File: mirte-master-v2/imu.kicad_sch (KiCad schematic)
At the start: 1 part, among them J8 IMU MPU-9250

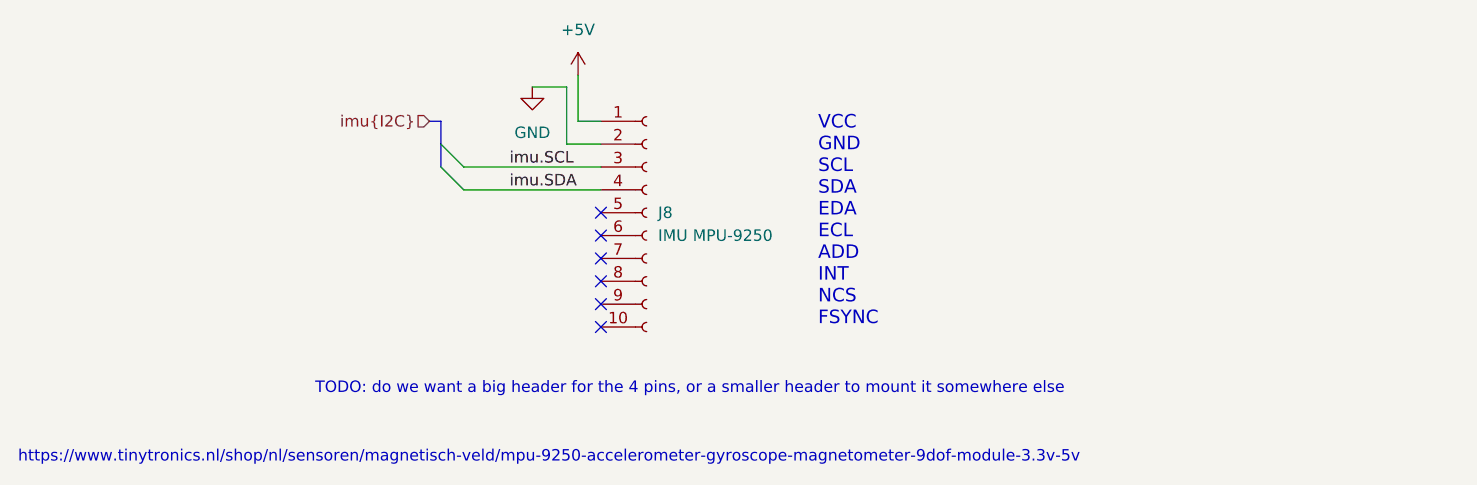
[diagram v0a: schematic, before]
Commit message: integrated the ina226 in the pcb layout
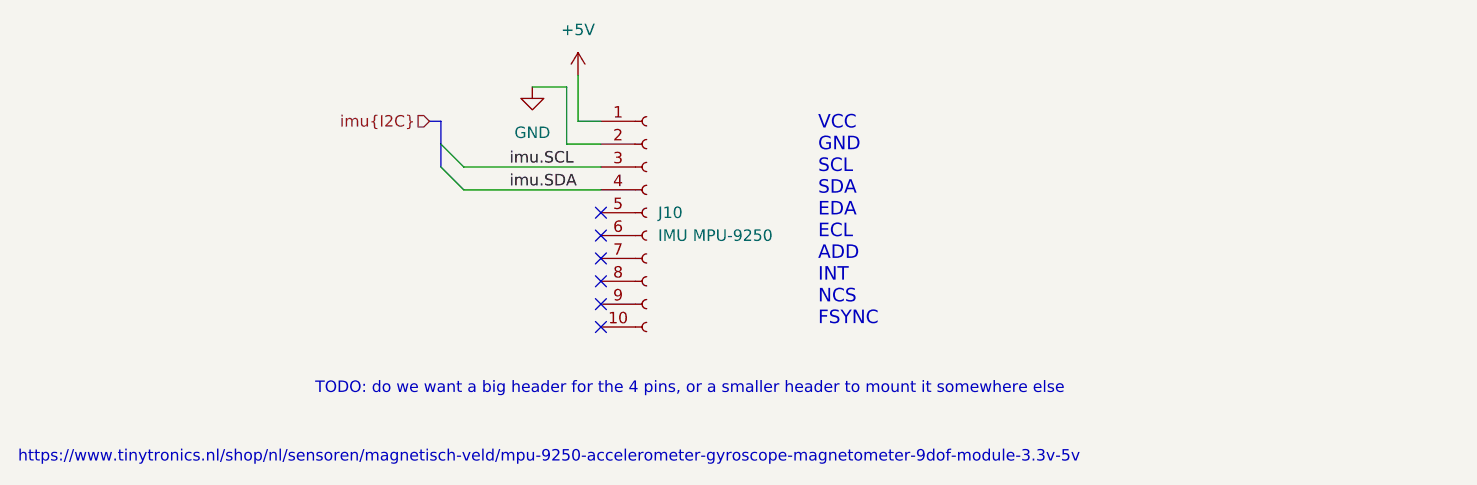
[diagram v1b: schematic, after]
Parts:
- renumbered J8 to J10
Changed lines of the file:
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@@
 		(dnp no)
 		(fields_autoplaced yes)
-		(property "Reference" "J8"
+		(property "Reference" "J10"
 			(at 132.08 72.39 0)
 			(effects
@@
 			(project "mirte-master"
 				(path "/19794465-0368-488c-958e-83b02754ebd6/75b0f62f-ad0e-4253-bb9a-0d4c3868edf5"
-					(reference "J8")
+					(reference "J10")
 					(unit 1)
 				)
